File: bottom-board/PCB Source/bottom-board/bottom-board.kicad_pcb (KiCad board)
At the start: 4 copper layers, 193 x 93 mm, 308 parts, among them J1 AS0A823-H4SB-7H, P1 USB_B, P10 JACK_TRS_6PINS, P11 JACK_TRS_6PINS, P12 JACK_TRS_6PINS, P13 RJ45, P14 AudioJack3, P2 USB_A, P3 BARREL_JACK, P5 HMI_DATA, P6 AudioJack3, P7 AudioJack3, P8 SERIAL_DEBUG, P9 JACK_TRS_6PINS, Q1 2N7002, Q10 MMBFJ110, Q12 2N7002, Q13 2N7002, Q2 2N7002, Q3 MMBFJ110, Q4 MMBFJ110, Q5 MMBFJ110, Q6 MMBFJ110, Q7 2N7002, Q8 2N7002, Q9 MMBFJ110, U1 TS2596, U10 TPS2001DDBVR, U11 6N137S, U12 ISL83491, U13 AP2120N-3.3, U2 TL750M10CKVURG3, U3 CS4265, U4 AT24CS08-STUM, U5 LM4562, U6 OPA1678, U7 OPA1678, U8 LM4811, U9 LD1117S50TR_SOT223, X1 24.576MHz

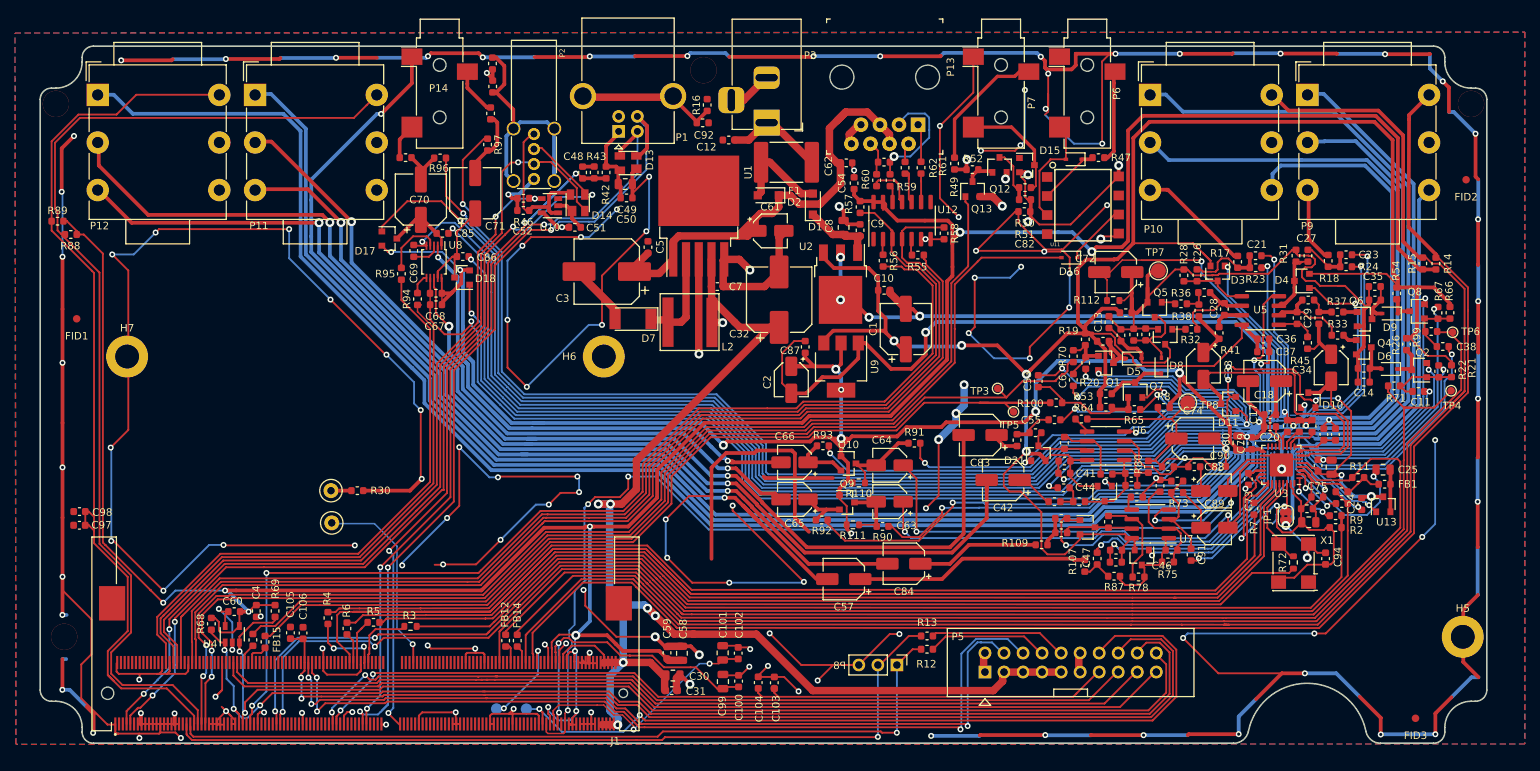
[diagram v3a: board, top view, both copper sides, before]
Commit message: move headphone jack up 0.5mm
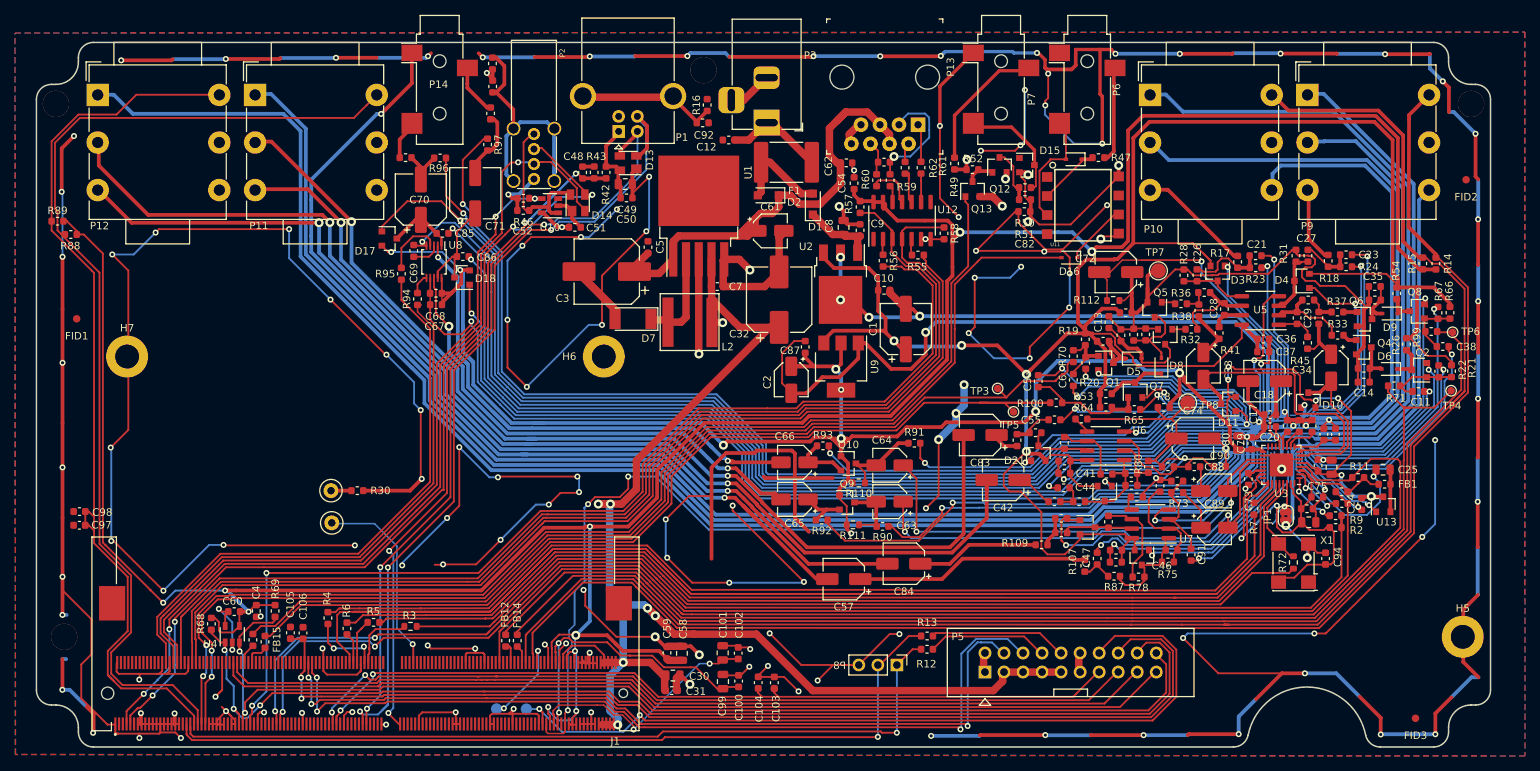
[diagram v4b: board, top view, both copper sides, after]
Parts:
- moved P14 0.50 mm to (112.7, 46.4)
- moved P6 0.50 mm to (199.1, 46.4)
- moved P7 0.50 mm to (187.6, 46.4)
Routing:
- net GNDD: track 1440.4 -> 1433.7 mm, vias 140 -> 141
- net Net-(P14-PadR): track 7.74 -> 6.32 mm
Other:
- board size 193 x 93 mm -> 194 x 94 mm

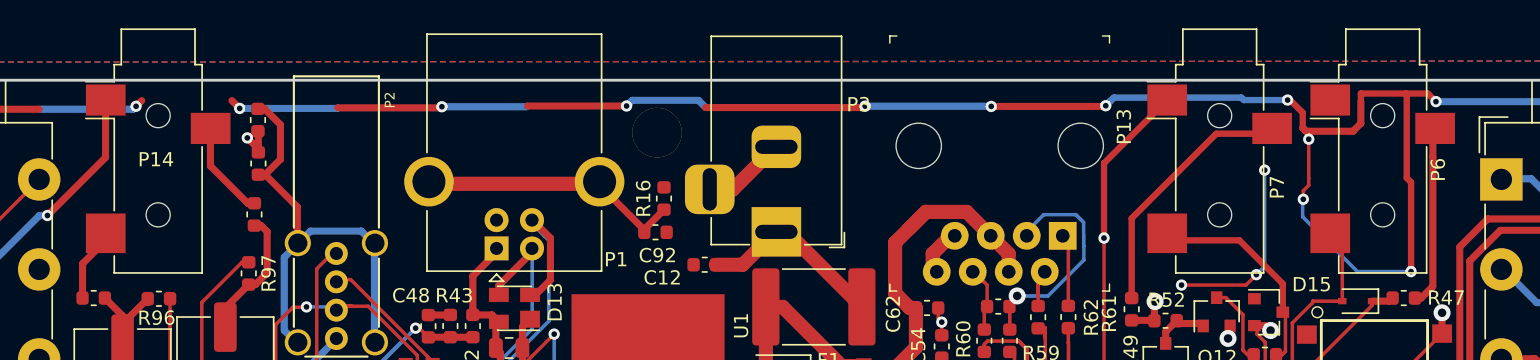
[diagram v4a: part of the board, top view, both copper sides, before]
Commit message: move mini jacks down 0.1mm
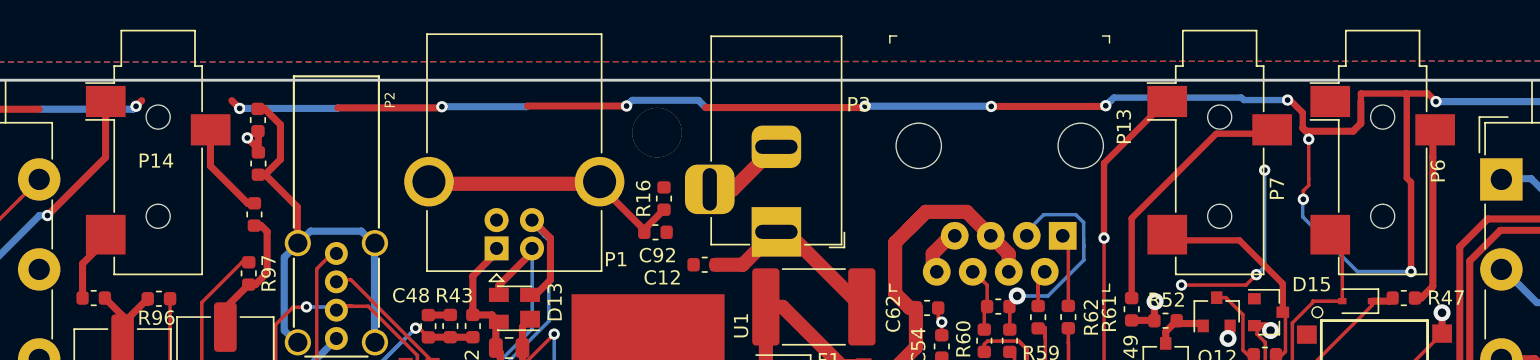
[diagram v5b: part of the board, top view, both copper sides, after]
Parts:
- moved P14 0.10 mm to (112.7, 46.5)
- moved P6 0.10 mm to (199.1, 46.5)
- moved P7 0.10 mm to (187.6, 46.5)
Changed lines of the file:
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@@
     )
   )
-  (module Connector_Audio:Jack_3.5mm_CUI_SJ-3523-SMT_Horizontal locked (layer F.Cu)
-    (at 199.11 46.43)
+  (module Connector_Audio:Jack_3.5mm_CUI_SJ-3523-SMT_Horizontal (layer F.Cu)
+    (at 199.11 46.53)
     (descr "3.5 mm, Stereo, Right Angle, Surface Mount (SMT), Audio Jack Connector (https://www.cui.com/product/resource/sj-352x-smt-series.pdf)")
     (tags "3.5mm audio cui horizontal jack stereo")
@@
     )
   )
-  (module Connector_Audio:Jack_3.5mm_CUI_SJ-3523-SMT_Horizontal locked (layer F.Cu)
-    (at 187.61 46.43)
+  (module Connector_Audio:Jack_3.5mm_CUI_SJ-3523-SMT_Horizontal (layer F.Cu)
+    (at 187.61 46.53)
     (descr "3.5 mm, Stereo, Right Angle, Surface Mount (SMT), Audio Jack Connector (https://www.cui.com/product/resource/sj-352x-smt-series.pdf)")
     (tags "3.5mm audio cui horizontal jack stereo")
@@
   )
   (module Connector_Audio:Jack_3.5mm_CUI_SJ-3523-SMT_Horizontal (layer F.Cu)
-    (at 112.71 46.43)
+    (at 112.71 46.53)
     (descr "3.5 mm, Stereo, Right Angle, Surface Mount (SMT), Audio Jack Connector (https://www.cui.com/product/resource/sj-352x-smt-series.pdf)")
     (tags "3.5mm audio cui horizontal jack stereo")

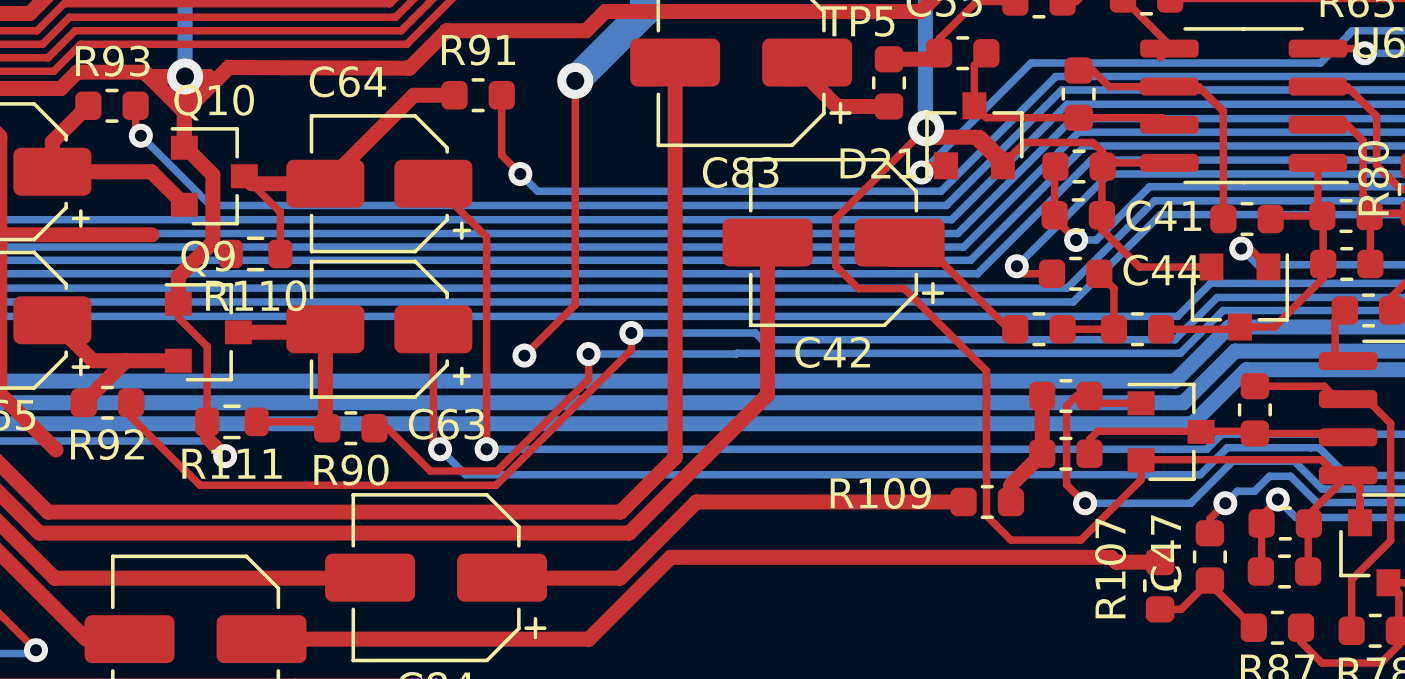
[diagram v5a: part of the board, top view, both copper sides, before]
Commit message: swap headphone L/R
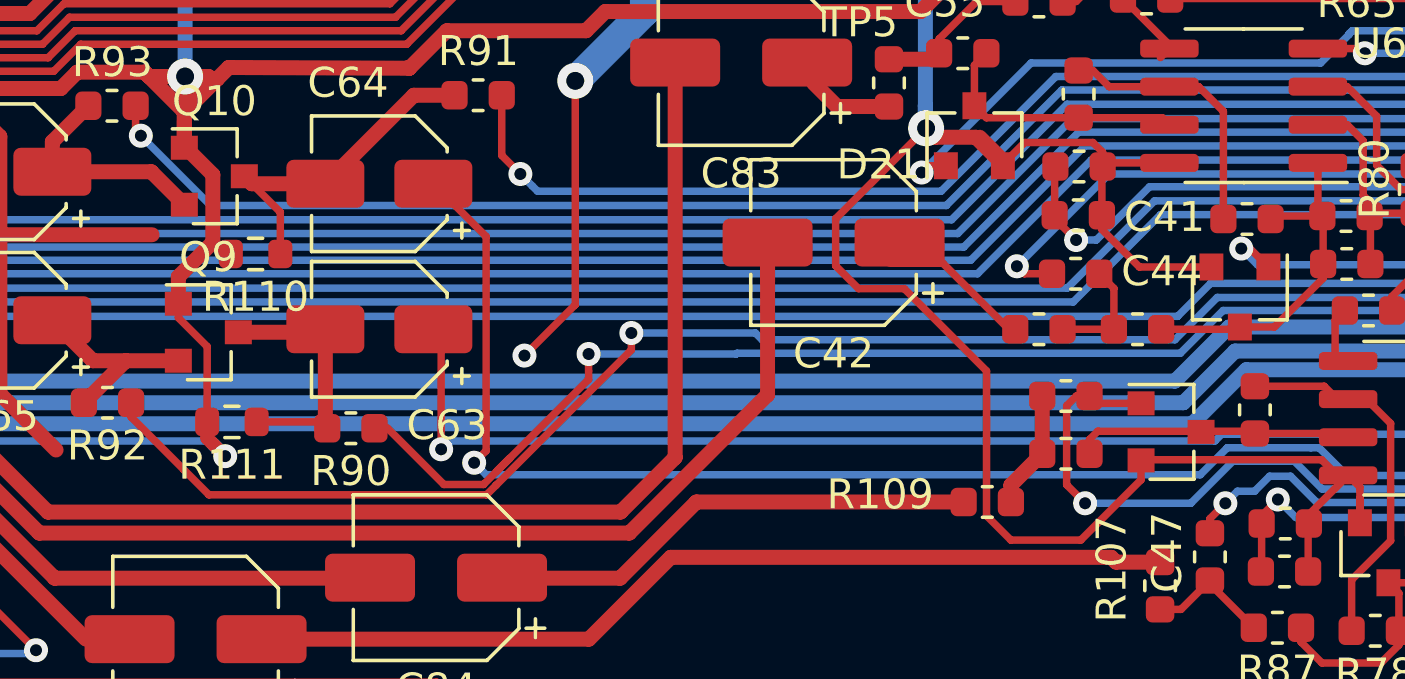
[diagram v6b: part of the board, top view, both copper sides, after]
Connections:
- C63 pad 1: CODEC_DAC_B -> CODEC_DAC_A
- C64 pad 1: CODEC_DAC_A -> CODEC_DAC_B
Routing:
- net CODEC_DAC_B: track 62.9 -> 67.7 mm
- net CODEC_DAC_A: track 62.7 -> 58.8 mm
- net GNDA: track 3564.7 -> 3565.9 mm
